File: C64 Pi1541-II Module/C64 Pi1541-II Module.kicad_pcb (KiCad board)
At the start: 2 copper layers, 87.6 x 97.8 mm, 31 parts, among them IC1 0.96_OLED, IC2 7406, IC3 I2C LC, J1 DC IN, J2 C64_IEC, J3 C64_IEC, J4 Faceplate, M1 Mounting, M2 Mounting, M3 Mounting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

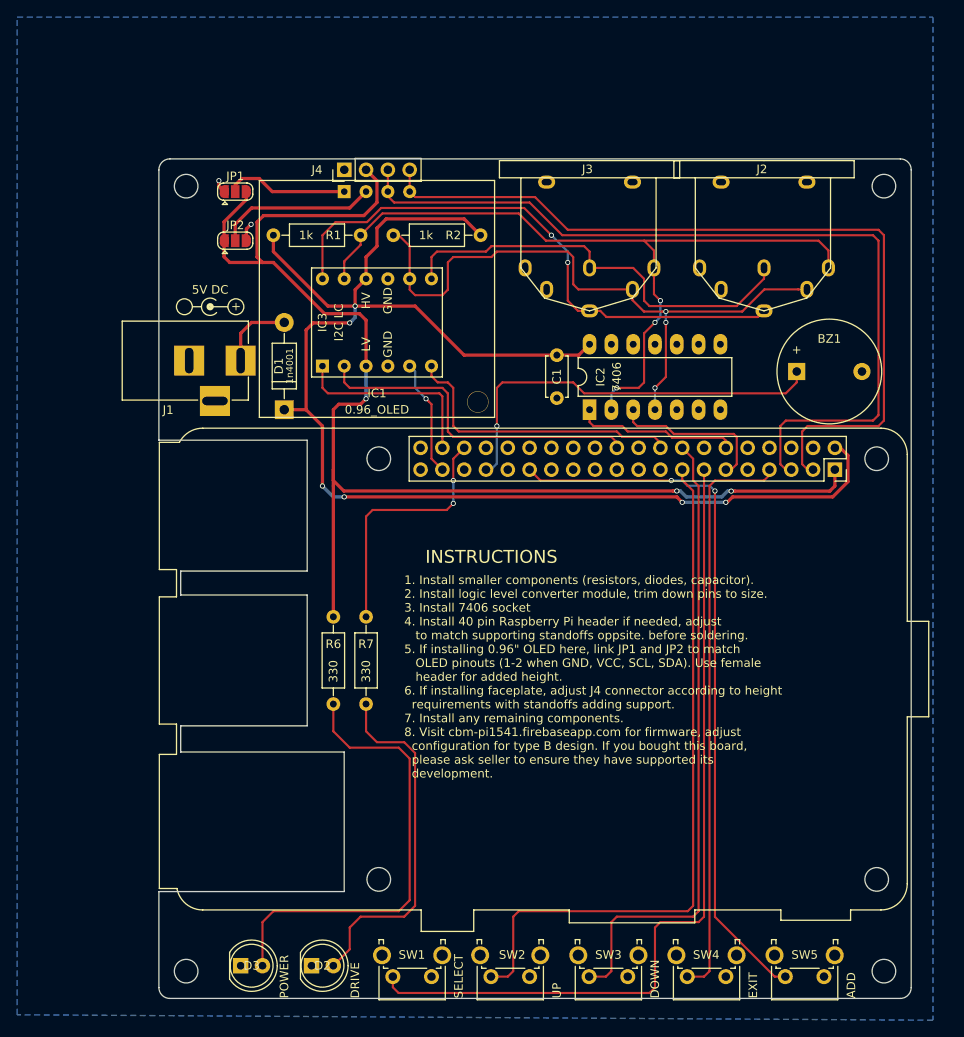
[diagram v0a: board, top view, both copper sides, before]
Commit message: Changed dimensions on module
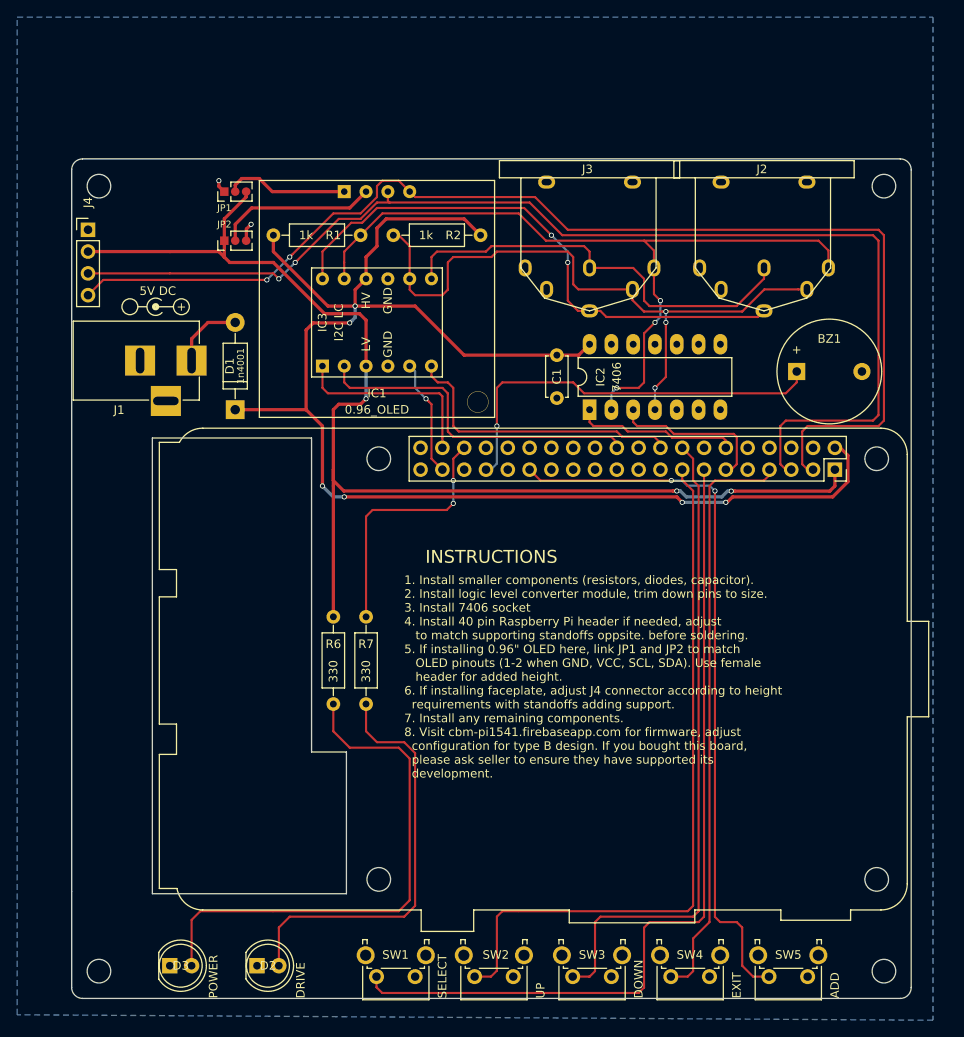
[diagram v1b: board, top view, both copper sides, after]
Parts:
- JP1, JP2: footprint Jumper:SolderJumper-3_P1.3mm_Open_RoundedPad1.0x1.5mm -> wire_pads:OLED_SEL
- moved J4 30.7 mm to (74.3, 62.9), turned to 0 degrees
- moved M1 10.2 mm to (75.6, 149.2)
- moved M4 10.2 mm to (75.6, 57.8)
- moved D3 8.26 mm to (83.8, 148.6)
- moved REF** 7.62 mm to (81.3, 74.4)
- moved REF** 6.35 mm to (82.2, 71.8)
- moved D2 6.35 mm to (94.0, 148.6)
- moved D1 5.72 mm to (91.4, 83.8)
- moved J1 5.72 mm to (86.4, 78.1)
- moved SW1 1.91 mm to (112.4, 149.9)
- moved SW2 1.91 mm to (123.8, 149.9)
- moved SW3 1.91 mm to (135.3, 149.9)
- moved SW4 1.91 mm to (146.7, 149.9)
- moved SW5 1.91 mm to (158.1, 149.9)
- moved JP1 1.27 mm to (90.2, 58.4), turned to 90 degrees
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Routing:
- net I2C_SDA: track 96.9 -> 138.6 mm, vias 0 -> 2
- net I2C_SCL: track 100.6 -> 138.1 mm, vias 0 -> 2
- net Net-(D3-Pad2): track 53.2 -> 61.6 mm
- net +3V3: track 153.0 -> 144.9 mm
- net Net-(D2-Pad2): track 41.6 -> 49.1 mm
- net +5V: track 164.8 -> 170.5 mm
- net SW3: track 74.0 -> 76.0 mm
- net SW1: track 97.6 -> 99.5 mm
- net SW2: track 82.0 -> 83.9 mm
- net C64_RST: track 66.7 -> 65.6 mm
- net SW4: track 67.5 -> 68.3 mm
- net SW5: track 83.3 -> 84.0 mm
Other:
- board size 87.6 x 97.8 mm -> 97.8 x 97.8 mm
- board text added: "Disk dimensions: 133.7mm PCB dimensions: 97,79mm Scale factor: 0.73"
- board text removed: "Disk dimensions: 133.7mm PCB dimensions: 78.6mm Scale factor: 0.59"

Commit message: Module silkscreen tweaks
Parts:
- added REF**: Symbol_Barrel_Polarity, Symbols:Symbol_Barrel_Polarity, F.Cu at (75.0, 87.6)
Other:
- board text added: "-"
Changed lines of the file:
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@@
   (general
     (thickness 1.6)
-    (drawings 23)
+    (drawings 28)
     (tracks 393)
     (zones 0)
-    (modules 31)
+    (modules 32)
     (nets 28)
   )
   (page A4)
   (layers
-    (0 F.Cu signal)
-    (31 B.Cu signal)
+    (0 F.Cu signal hide)
+    (31 B.Cu signal hide)
     (32 B.Adhes user)
     (33 F.Adhes user)
@@
     (uvia_dia 0.3)
     (uvia_drill 0.1)
+  )
+  (module Symbols:Symbol_Barrel_Polarity (layer F.Cu)
+    (at 75.005 87.63 270)
+    (descr "Barrel connector polarity indicator")
+    (tags "barrel polarity")
+    (fp_text reference REF** (at 0 -2 90) (layer F.SilkS) hide
+      (effects (font (size 1 1) (thickness 0.15)))
+    )
+    (fp_text value Symbol_Barrel_Polarity (at 0 2 90) (layer F.Fab)
+      (effects (font (size 1 1) (thickness 0.15)))
+    )
+    (fp_line (start 0 0.075) (end 2 0.075) (layer F.SilkS) (width 0.15))
+    (fp_line (start -2 0.075) (end -1.1 0.075) (layer F.SilkS) (width 0.15))
+    (fp_circle (center -3 0.075) (end -3 1) (layer F.SilkS) (width 0.15))
+    (fp_circle (center 3 0.075) (end 3 1) (layer F.SilkS) (width 0.15))
+    (fp_circle (center 0 0.075) (end 0 0.25) (layer F.SilkS) (width 0.5))
+    (fp_arc (start 0 0.075) (end 0.75 0.75) (angle 270) (layer F.SilkS) (width 0.15))
   )
   (module Buttons_Switches_THT:SW_Tactile_SPST_Angled_PTS645Vx39-2LFS (layer F.Cu)
@@
     (descr "DC Barrel Jack")
     (tags "Power Jack")
-    (fp_text reference J1 (at -8.45 5.75 180) (layer F.SilkS)
+    (fp_text reference J1 (at -6.35 3.175 180) (layer F.SilkS)
       (effects (font (size 1 1) (thickness 0.15)))
     )
@@
     (descr "Through hole straight pin header, 1x03, 1.27mm pitch, single row")
     (tags "Through hole pin header THT 1x03 1.27mm single row")
-    (fp_text reference JP1 (at -1.905 0 180) (layer F.SilkS)
+    (fp_text reference JP1 (at 0 -1.905 270) (layer F.SilkS)
       (effects (font (size 0.8 0.8) (thickness 0.1)))
     )
-    (fp_text value P1_GND (at 0 4.445 90) (layer F.Fab)
+    (fp_text value P1_GND (at 1.905 1.27 180) (layer F.Fab)
       (effects (font (size 0.8 0.8) (thickness 0.1)))
     )
@@
     (descr "Through hole straight pin header, 1x03, 1.27mm pitch, single row")
     (tags "Through hole pin header THT 1x03 1.27mm single row")
-    (fp_text reference JP2 (at 1.905 0 180) (layer F.SilkS)
+    (fp_text reference JP2 (at 0 -1.905 270) (layer F.SilkS)
       (effects (font (size 0.8 0.8) (thickness 0.1)))
     )
-    (fp_text value P2_VCC (at 0 4.445 90) (layer F.Fab)
+    (fp_text value P2_VCC (at 1.905 1.27 180) (layer F.Fab)
       (effects (font (size 0.8 0.8) (thickness 0.1)))
     )
@@
     )
   )
+  (gr_text - (at 78.3336 74.3966 180) (layer B.SilkS)
+    (effects (font (size 1 1) (thickness 0.15)) (justify mirror))
+  )
+  (gr_text - (at 79.1464 71.755) (layer F.SilkS)
+    (effects (font (size 1 1) (thickness 0.15)))
+  )
+  (gr_text - (at 75.0062 84.6328 270) (layer F.SilkS)
+    (effects (font (size 1 1) (thickness 0.15)))
+  )
+  (gr_text + (at 74.93 90.63 270) (layer F.SilkS)
+    (effects (font (size 1 1) (thickness 0.15)))
+  )
+  (gr_text "5V DC" (at 76.765 87.882 270) (layer F.SilkS)
+    (effects (font (size 1 1) (thickness 0.15)))
+  )
   (gr_text "5V DC" (at 82.421 69.995) (layer F.SilkS)

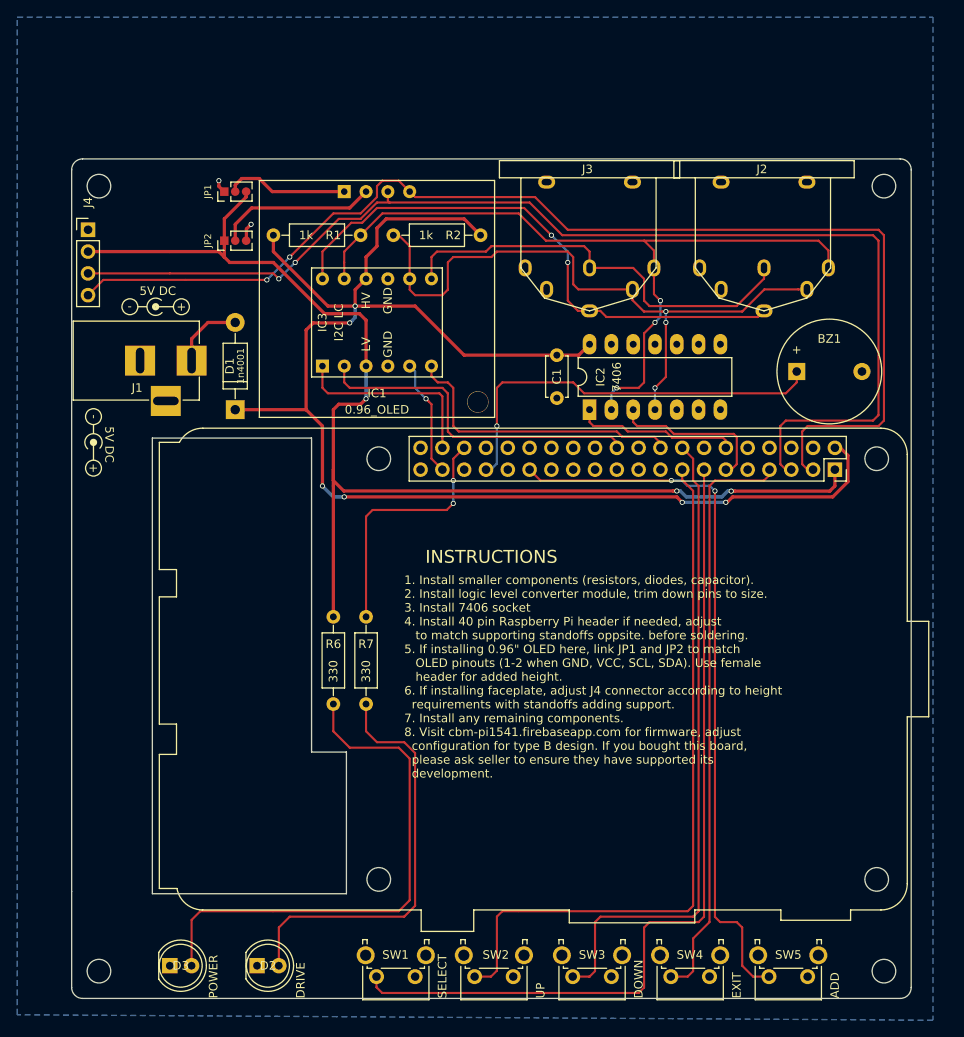
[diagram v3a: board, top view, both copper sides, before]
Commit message: Removed diode
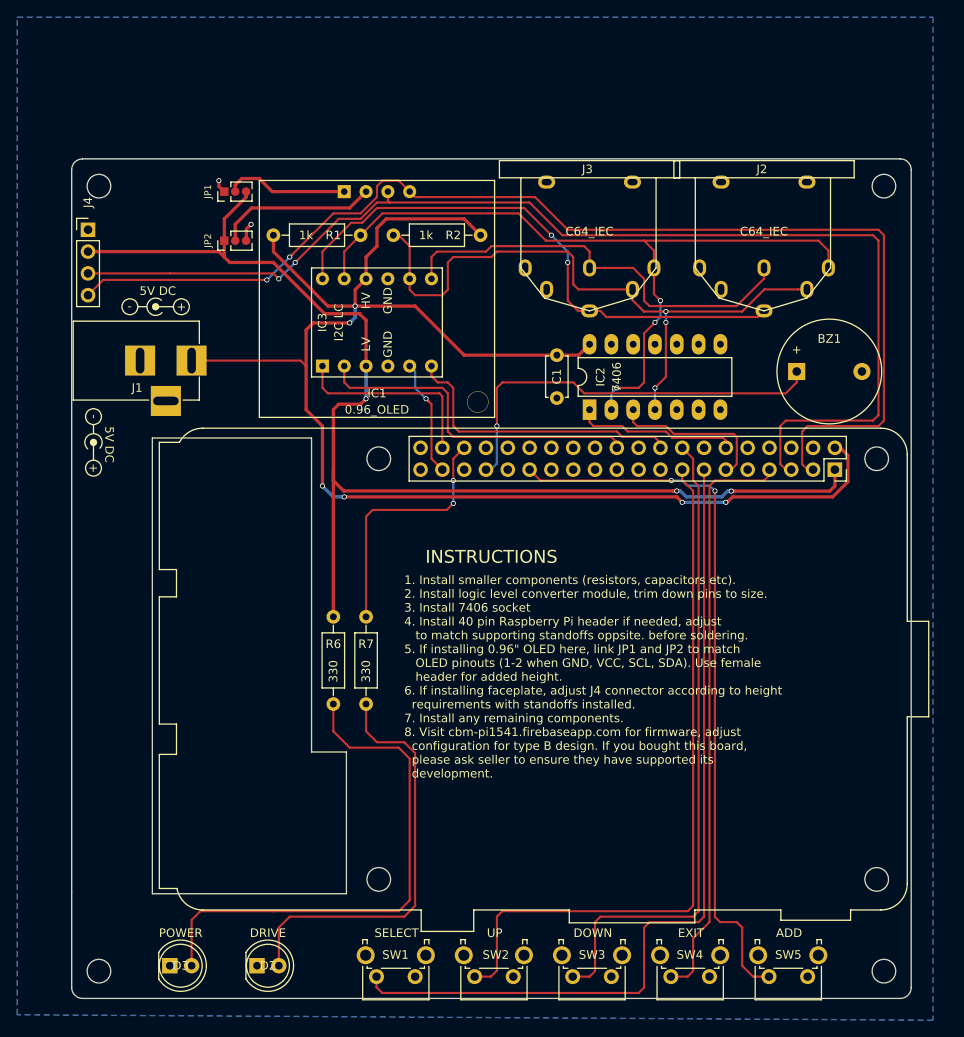
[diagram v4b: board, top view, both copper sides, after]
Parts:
- removed D1: 1n4001, Diodes_THT:D_DO-41_SOD81_P10.16mm_Horizontal
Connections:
- J1 pad 1: Net-(D1-Pad2) -> +5V
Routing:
- net Net-(D1-Pad2): track 8.41 -> 0.00 mm
- net +5V: track 170.5 -> 175.8 mm
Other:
- board text added: "1. Install smaller components (resistors, capacitors etc). 2. Install logic level converter module, trim down pins to size. 3. Install 7406 socket 4. Install 40 pin Raspberry Pi header if needed, adjust to match supporting standoffs oppsite. before soldering. 5. If installing 0.96" OLED here, link JP1 and JP2 to match OLED pinouts (1-2 when GND, VCC, SCL, SDA). Use female header for added height.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"
- board text removed: "1. Install smaller components (resistors, diodes, capacitor). 2. Install logic level converter module, trim down pins to size. 3. Install 7406 socket 4. Install 40 pin Raspberry Pi header if needed, adjust to match supporting standoffs oppsite. before soldering. 5. If installing 0.96" OLED here, link JP1 and JP2 to match OLED pinouts (1-2 when GND, VCC, SCL, SDA). Use female header for added heig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"
